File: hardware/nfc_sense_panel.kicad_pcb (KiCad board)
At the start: 4 copper layers, 121 x 105.3 mm, 740 parts, among them U1 TMP117AIDRVR, U2 RF430CL330HIRGTR‎, U3 ATtiny1626-MFR

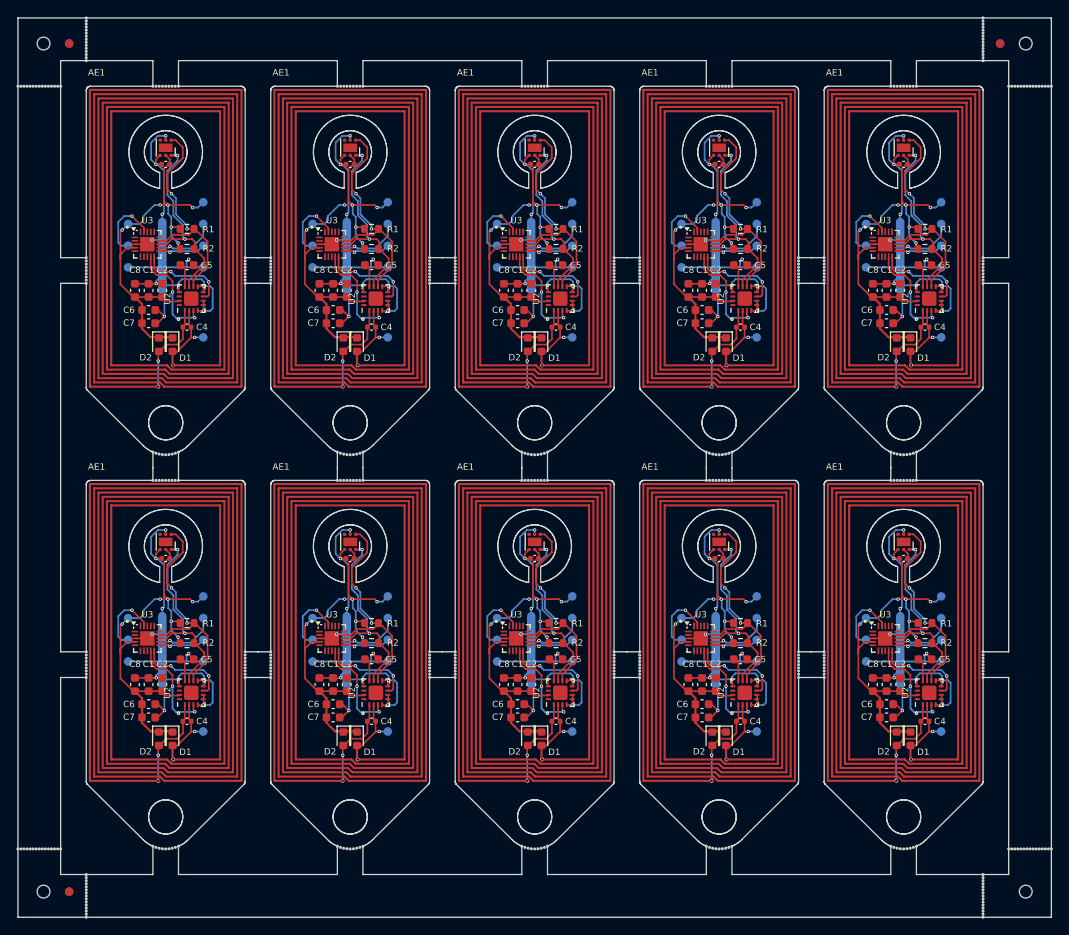
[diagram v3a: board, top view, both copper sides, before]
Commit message: update panel + panel settings
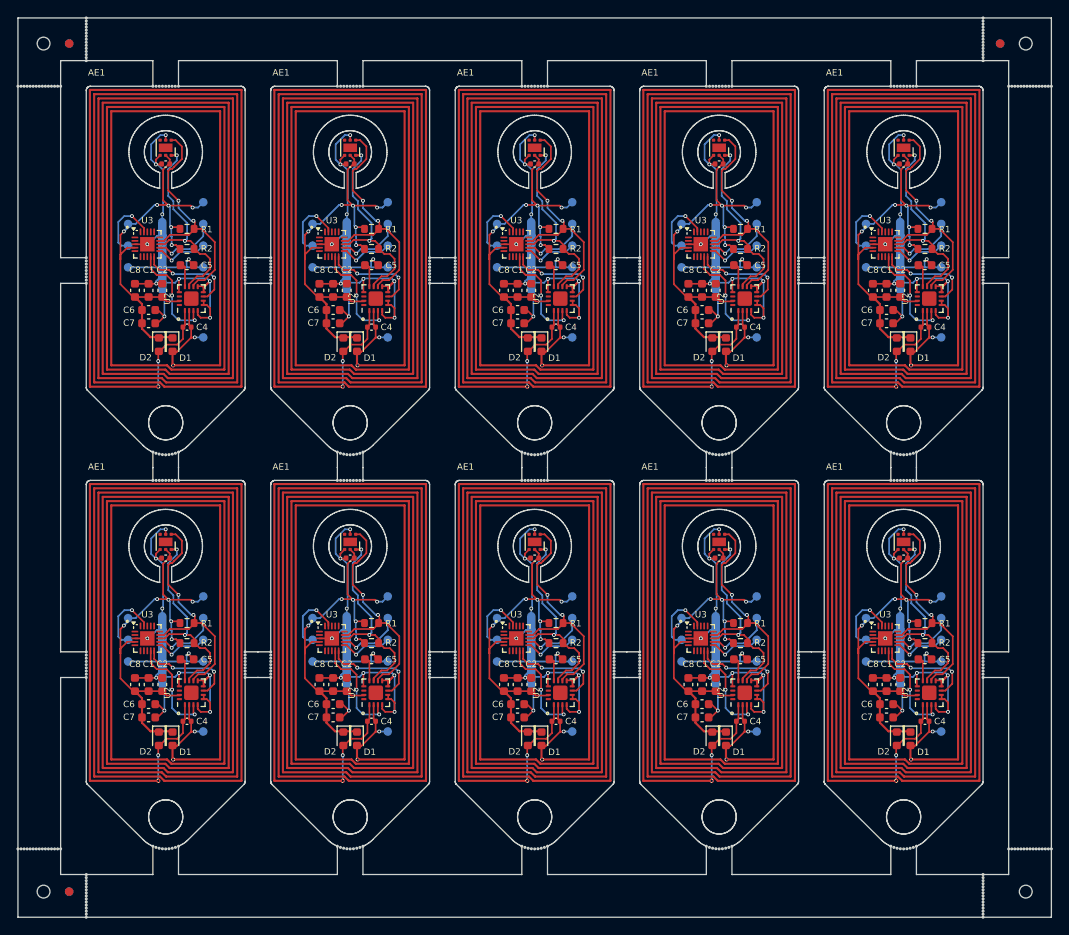
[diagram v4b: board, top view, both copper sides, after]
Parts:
- removed the C3 at (191.7, 37.2)
- removed the C3 at (105.3, 37.2)
- removed the C3 at (105.3, 83.3)
- removed the C3 at (148.5, 83.3)
- removed the C3 at (148.5, 37.2)
- removed the C3 at (170.1, 83.3)
- removed the C3 at (126.9, 83.3)
- removed the C3 at (191.7, 83.3)
- removed the C3 at (170.1, 37.2)
- removed the C3 at (126.9, 37.2)
- added C3: 0.1 uF, Capacitor_SMD:C_0402_1005Metric, F.Cu at (105.3, 37.1)
- added C3: 0.1 uF, Capacitor_SMD:C_0402_1005Metric, F.Cu at (126.9, 83.2)
- added C3: 0.1 uF, Capacitor_SMD:C_0402_1005Metric, F.Cu at (170.1, 37.1)
- added C3: 0.1 uF, Capacitor_SMD:C_0402_1005Metric, F.Cu at (170.1, 83.2)
- added C3: 0.1 uF, Capacitor_SMD:C_0402_1005Metric, F.Cu at (105.3, 83.2)
- added C3: 0.1 uF, Capacitor_SMD:C_0402_1005Metric, F.Cu at (191.7, 37.1)
- added C3: 0.1 uF, Capacitor_SMD:C_0402_1005Metric, F.Cu at (126.9, 37.1)
- added C3: 0.1 uF, Capacitor_SMD:C_0402_1005Metric, F.Cu at (148.5, 83.2)
- added C3: 0.1 uF, Capacitor_SMD:C_0402_1005Metric, F.Cu at (191.7, 83.2)
- added C3: 0.1 uF, Capacitor_SMD:C_0402_1005Metric, F.Cu at (148.5, 37.1)
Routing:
- net Board_8-GND: track 62.0 -> 68.1 mm
- net Board_5-GND: track 62.0 -> 68.1 mm
- net Board_6-GND: track 62.0 -> 68.1 mm
- net Board_9-GND: track 62.0 -> 68.1 mm
- net Board_7-GND: track 62.0 -> 68.1 mm
- net Board_3-GND: track 62.0 -> 68.1 mm
- net Board_4-GND: track 62.0 -> 68.1 mm
- net Board_0-GND: track 62.0 -> 68.1 mm
- net Board_1-GND: track 62.0 -> 68.1 mm
- net Board_2-GND: track 62.0 -> 68.1 mm
- net Board_7-SDA: track 22.8 -> 24.0 mm
- net Board_9-SDA: track 22.8 -> 24.0 mm
- net Board_2-SDA: track 22.8 -> 24.0 mm
- net Board_4-SDA: track 22.8 -> 24.0 mm
- net Board_6-SDA: track 22.8 -> 24.0 mm
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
